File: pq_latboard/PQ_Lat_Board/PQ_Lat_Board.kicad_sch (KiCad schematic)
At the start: 20 parts, among them IC1 TCN75AVOA713, J1 Conn_01x11_MountingPin, J2 Conn_Coaxial

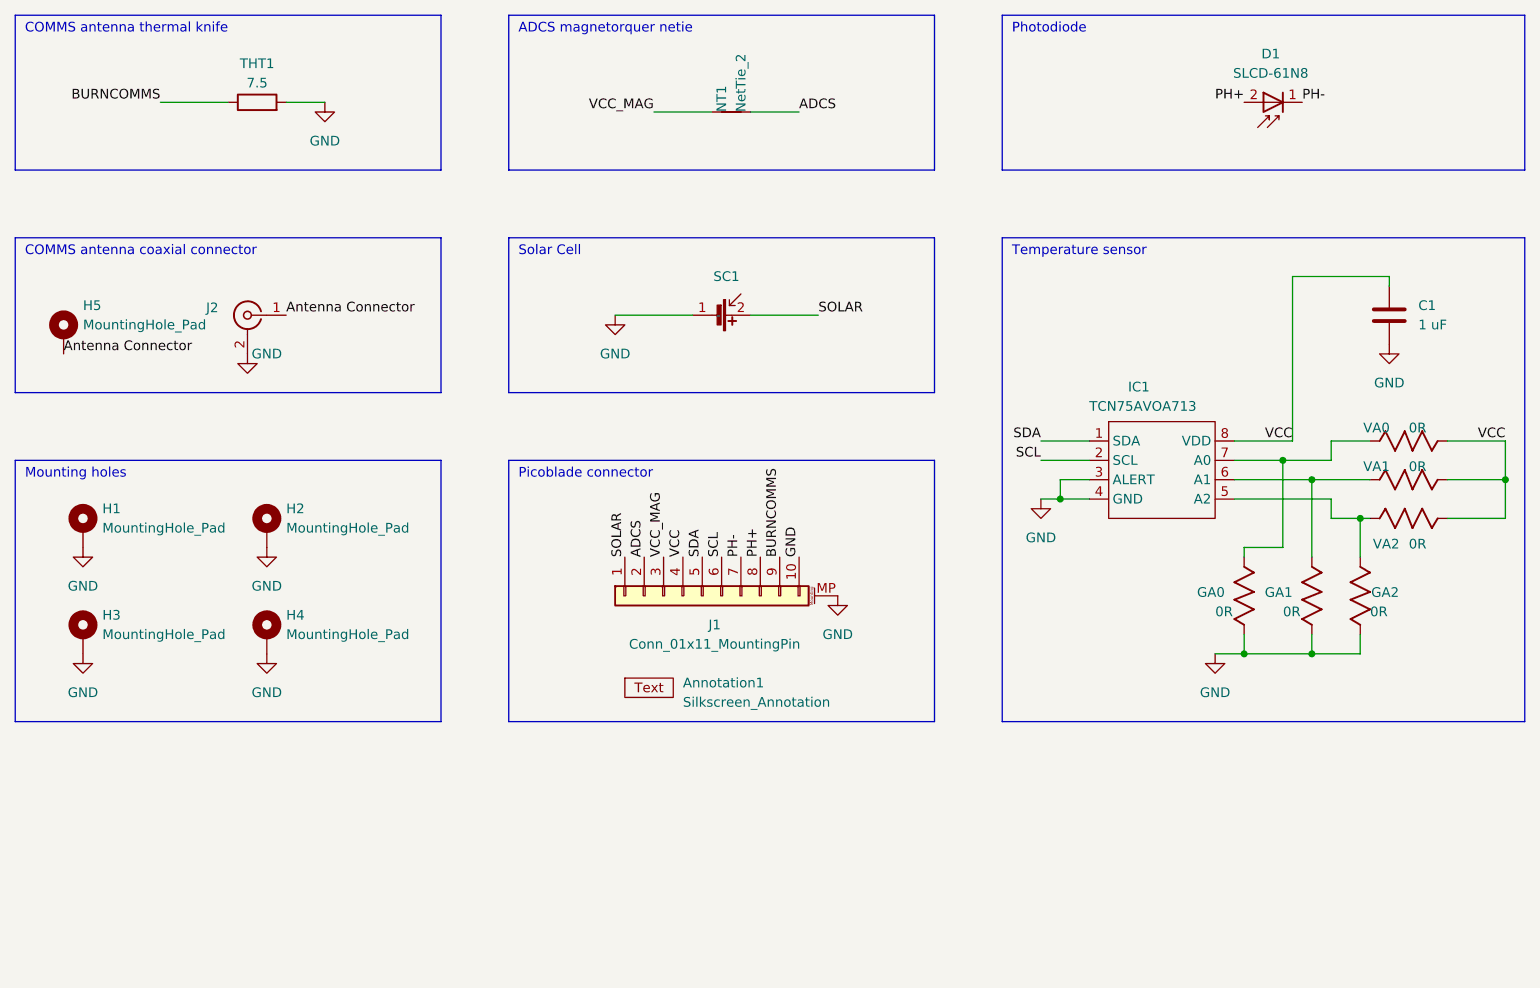
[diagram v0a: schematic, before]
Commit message: add names, bigger hole and mirror solar cell
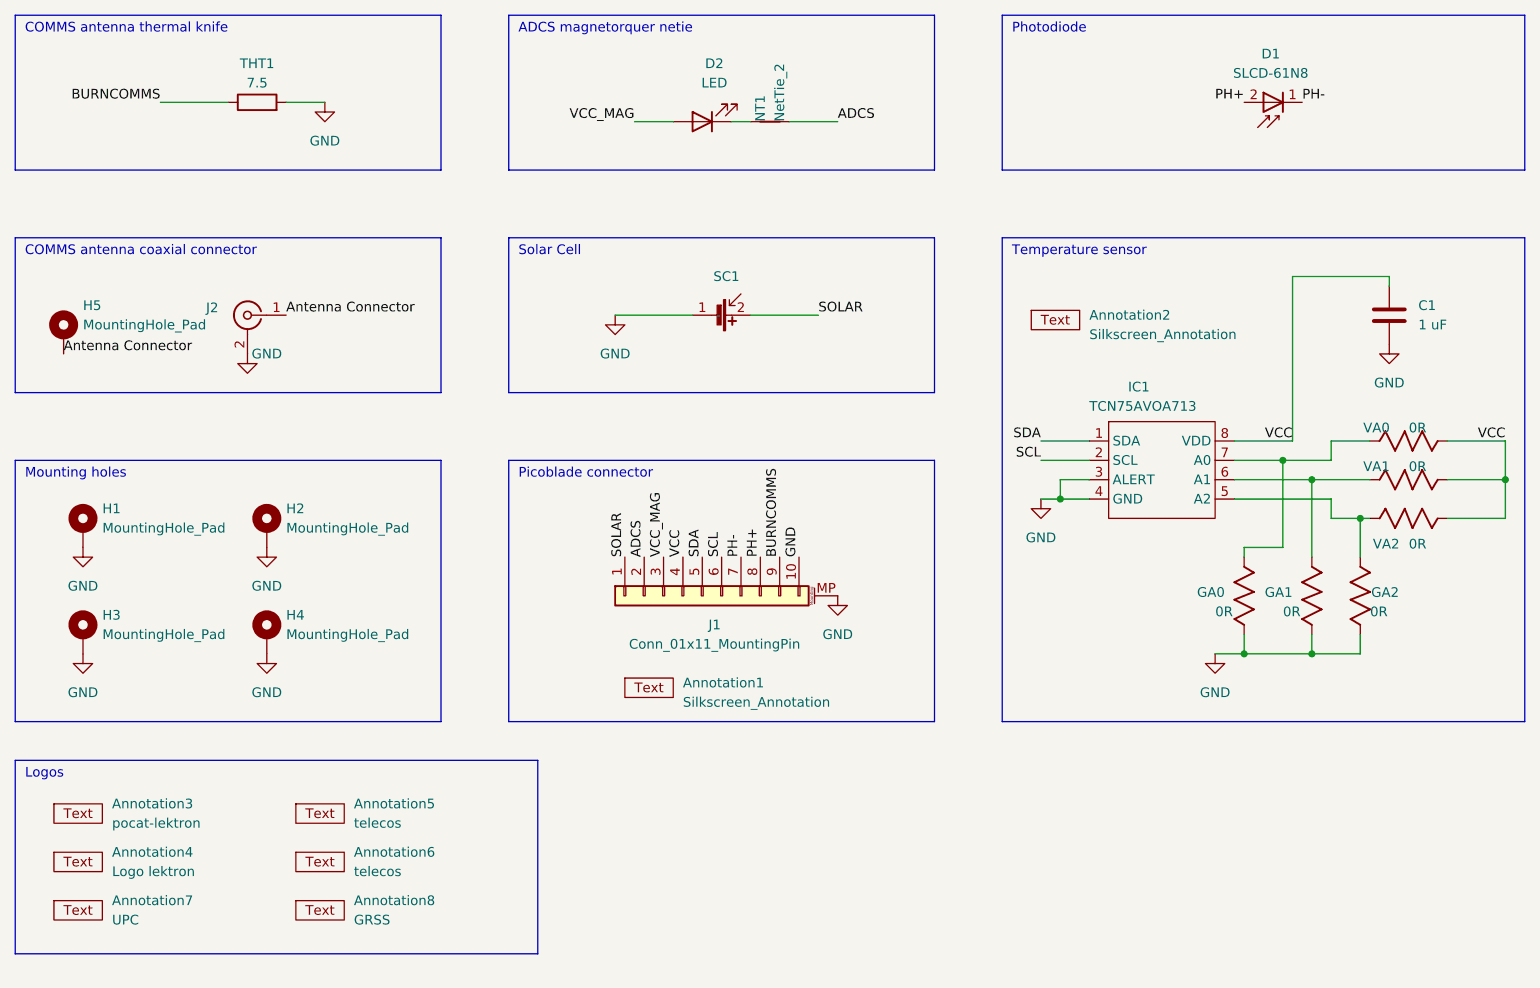
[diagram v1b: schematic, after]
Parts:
- added Annotation2: Silkscreen_Annotation, symbols-nsl:snail, symbol -nsl_symbols:Silkscreen_Annotation
- added Annotation3: pocat-lektron, symbols-nsl:pocat-lektron, symbol -nsl_symbols:Silkscreen_Annotation
- added Annotation4: Logo lektron, symbols-nsl:logo_pq, symbol -nsl_symbols:Silkscreen_Annotation
- added Annotation5: telecos, symbols-nsl:Telecos, symbol -nsl_symbols:Silkscreen_Annotation
- added Annotation6: telecos, symbols-nsl:NSL-small, symbol -nsl_symbols:Silkscreen_Annotation
- added Annotation7: UPC, symbols-nsl:UPC_small, symbol -nsl_symbols:Silkscreen_Annotation
- added Annotation8: GRSS, symbols-nsl:GRSS, symbol -nsl_symbols:Silkscreen_Annotation
- added D2: LED, LED_SMD:LED_0402_1005Metric, symbol Device:LED
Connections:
- net VCC_MAG: now also D2.2 (A); no longer NT1.1
- new net: D2.1 (K), NT1.1
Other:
- note added: "Logos"
- moved on the sheet: NT1

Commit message: Removed netie, updated SC footprint, trace reform, logo&name cleanup, footprint reconciled, DRC
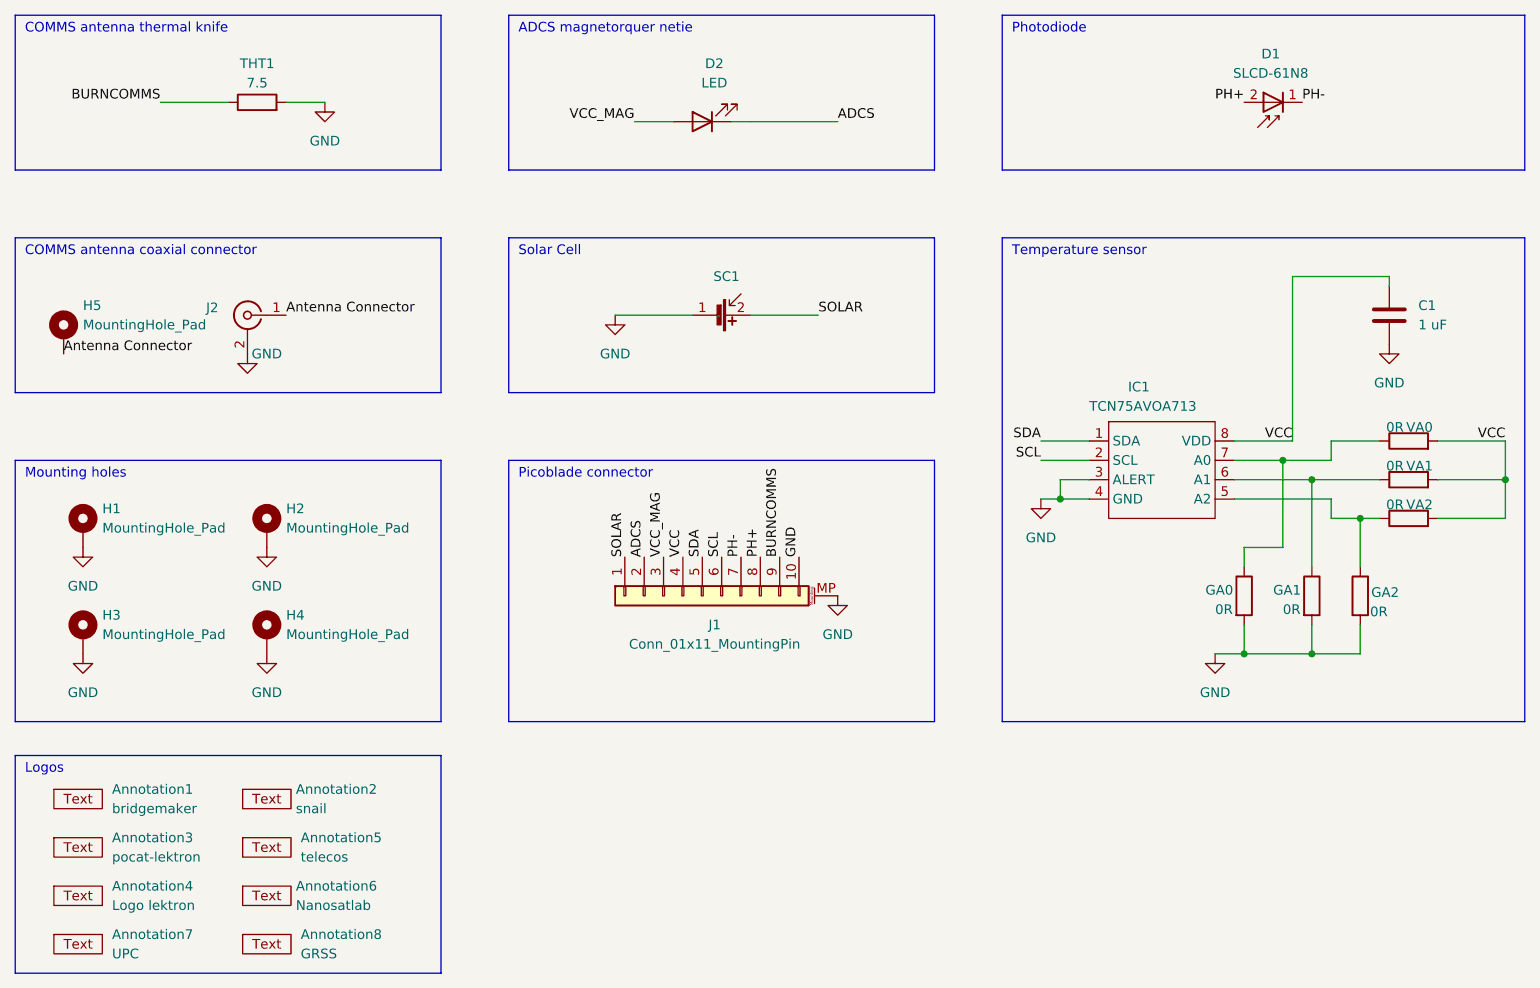
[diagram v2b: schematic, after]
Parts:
- removed NT1: NetTie_2, NetTie:NetTie-2_SMD_Pad0.5mm, symbol Device:NetTie_2
- Annotation1: value Silkscreen_Annotation -> bridgemaker; footprint -nsl_symbols:Bridgemaker -> symbols-nsl:Bridgemaker
- Annotation2: value Silkscreen_Annotation -> snail; footprint symbols-nsl:snail -> symbols-nsl:Snail
- Annotation3: footprint symbols-nsl:pocat-lektron -> symbols-nsl:pocat_lektron
- Annotation4: footprint symbols-nsl:logo_pq -> symbols-nsl:NSL_hexagon
- Annotation6: value telecos -> Nanosatlab
- D1: footprint -nsl_passive:SLCD-61N8 -> passive-nsl:SLCD-61N8
- GA0, GA1, GA2: symbol Lateral_board-altium-import:1_5k -> Device:R
- IC1: footprint -nsl_sensor:TCN75AVOA -> sensor-nsl:TCN75AVOA
- VA0, VA1, VA2: symbol Lateral_board-altium-import:0_5k -> Device:R
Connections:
- net ADCS: now also D2.1 (K)
- net GND: now also GA0.2, GA1.2, GA2.2; no longer GA0.1, GA1.1, GA2.1
- net at IC1.7 (A0), VA0.1: now also GA0.1; no longer GA0.2
- net at IC1.6 (A1), VA1.1: now also GA1.1; no longer GA1.2
- net at IC1.5 (A2), VA2.1: now also GA2.1; no longer GA2.2
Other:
- moved on the sheet: Annotation1, Annotation2, Annotation3, Annotation4, Annotation5, Annotation6, Annotation7, Annotation8

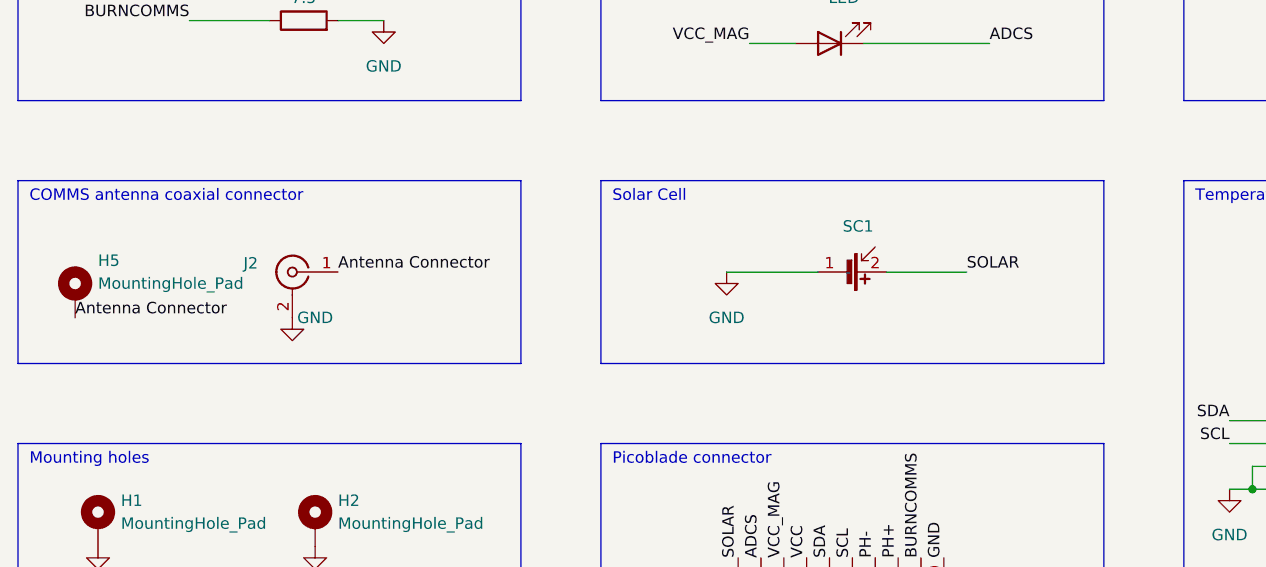
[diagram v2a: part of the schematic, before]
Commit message: Re-routed the SC, added new SC symbol in schematic, and added pad to solder the comms antenna inside the lateral.
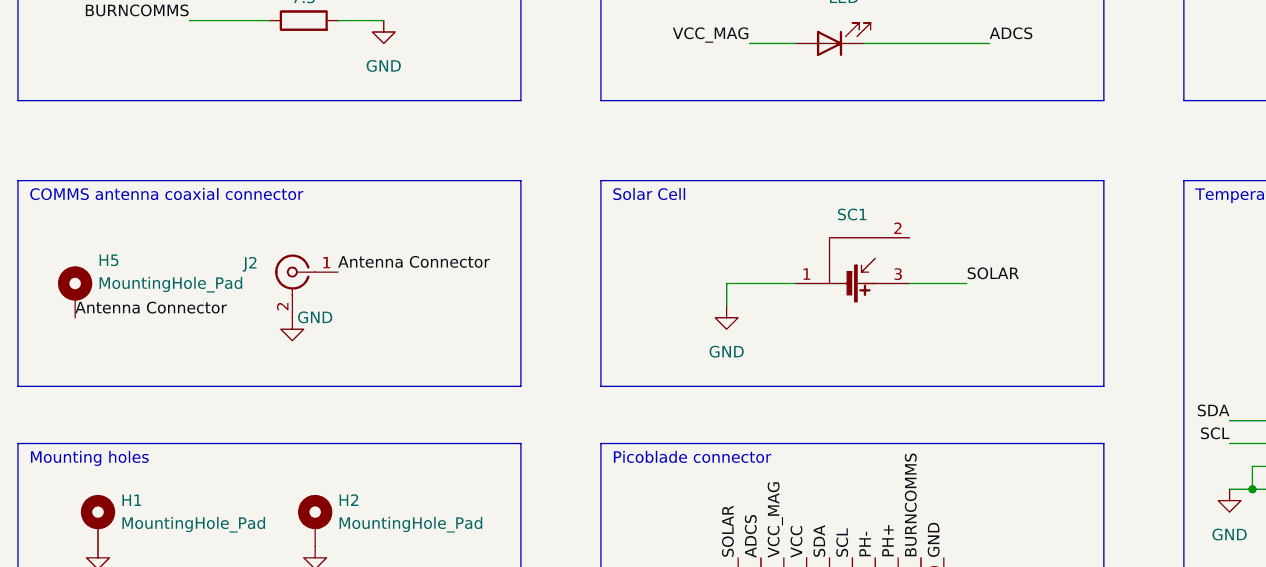
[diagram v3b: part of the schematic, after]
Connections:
- net SOLAR: now also SC1.3; no longer SC1.2
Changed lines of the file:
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@@
     (stroke (width 0.254) (type default))
   )
-  (polyline (pts (xy 114.3 82.55) (xy 114.3 102.87))
+  (polyline (pts (xy 114.3 82.55) (xy 114.3 105.41))
     (stroke (width 0) (type default))
   )
@@
     (stroke (width 0) (type default))
   )
-  (wire (pts (xy 128.27 92.71) (xy 138.43 92.71))
-    (stroke (width 0) (type default))
-  )
-  (polyline (pts (xy 114.3 102.87) (xy 170.18 102.87))
+  (polyline (pts (xy 114.3 105.41) (xy 170.18 105.41))
     (stroke (width 0) (type default))
   )
@@
     (stroke (width 0) (type default))
   )
-  (wire (pts (xy 146.05 92.71) (xy 154.94 92.71))
+  (wire (pts (xy 135.89 93.98) (xy 128.27 93.98))
     (stroke (width 0) (type default))
   )
@@
     (stroke (width 0.254) (type default))
   )
-  (polyline (pts (xy 170.18 82.55) (xy 170.18 102.87))
+  (polyline (pts (xy 170.18 82.55) (xy 170.18 105.41))
     (stroke (width 0) (type default))
   )
@@
     (stroke (width 0) (type default))
   )
+  (wire (pts (xy 128.27 93.98) (xy 128.27 96.52))
+    (stroke (width 0) (type default))
+  )
+  (wire (pts (xy 148.59 93.98) (xy 154.94 93.98))
+    (stroke (width 0) (type default))
+  )
   (wire (pts (xy 143.51 67.31) (xy 146.05 67.31))
     (stroke (width 0) (type default))
@@
     (stroke (width 0) (type default))
   )
-  (polyline (pts (xy 49.53 82.55) (xy 49.53 102.87))
+  (polyline (pts (xy 49.53 82.55) (xy 49.53 105.41))
     (stroke (width 0) (type default))
   )
@@
     (stroke (width 0) (type default))
   )
-  (polyline (pts (xy 105.41 102.87) (xy 105.41 82.55))
+  (polyline (pts (xy 105.41 105.41) (xy 105.41 82.55))
     (stroke (width 0) (type default))
   )
@@
     (stroke (width 0.254) (type default))
   )
-  (polyline (pts (xy 49.53 102.87) (xy 105.41 102.87))
+  (polyline (pts (xy 49.53 105.41) (xy 105.41 105.41))
     (stroke (width 0) (type default))
   )
@@
     (effects (font (size 1.27 1.27)) (justify left bottom))
   )
-  (label "SOLAR" (at 154.94 92.71 0) (fields_autoplaced)
+  (label "SOLAR" (at 154.94 93.98 0) (fields_autoplaced)
     (effects (font (size 1.27 1.27)) (justify left bottom))
   )
@@
     )
   )
-  (symbol (lib_name "GND_2") (lib_id "power:GND") (at 128.27 92.71 0) (unit 1)
-    (in_bom yes) (on_board yes) (dnp no) (fields_autoplaced)
-    (property "Reference" "#PWR0111" (at 128.27 99.06 0)
-      (effects (font (size 1.27 1.27)) hide)
-    )
-    (property "Value" "GND" (at 128.27 97.79 0)
-      (effects (font (size 1.27 1.27)))
-    )
-    (property "Footprint" "" (at 128.27 92.71 0)
-      (effects (font (size 1.27 1.27)) hide)
-    )
-    (property "Datasheet" "" (at 128.27 92.71 0)
+  (symbol (lib_name "GND_2") (lib_id "power:GND") (at 128.27 96.52 0) (unit 1)
+    (in_bom yes) (on_board yes) (dnp no) (fields_autoplaced)
+    (property "Reference" "#PWR0111" (at 128.27 102.87 0)
+      (effects (font (size 1.27 1.27)) hide)
+    )
+    (property "Value" "GND" (at 128.27 101.6 0)
+      (effects (font (size 1.27 1.27)))
+    )
+    (property "Footprint" "" (at 128.27 96.52 0)
+      (effects (font (size 1.27 1.27)) hide)
+    )
+    (property "Datasheet" "" (at 128.27 96.52 0)
       (effects (font (size 1.27 1.27)) hide)
     )
@@
     )
   )
+  (symbol (lib_id "power-nsl:S3040_CIC") (at 142.24 93.98 270) (unit 1)
+    (in_bom yes) (on_board yes) (dnp no) (fields_autoplaced)
+    (property "Reference" "SC1" (at 142.24 86.36 90)
+      (effects (font (size 1.27 1.27)))
+    )
+    (property "Value" "~" (at 142.24 93.98 0)
+      (effects (font (size 1.27 1.27)))
+    )
+    (property "Footprint" "power-nsl:Lighttricity_S3040_CIC" (at 142.24 93.98 0)
+      (effects (font (size 1.27 1.27)) hide)
+    )
+    (property "Datasheet" "" (at 142.24 93.98 0)
+      (effects (font (size 1.27 1.27)) hide)
+    )
+    (pin "2")
+    (pin "1")
+    (pin "3")
+    (instances
+      (project "PQ_Lat_Board"
+        (path "/4da848d5-e65a-4ace-88f8-d9d6d6b9afa2"
+          (reference "SC1") (unit 1)
+        )
+      )
+    )
+  )
   (symbol (lib_id "-nsl_symbols:Silkscreen_Annotation") (at 55.88 168.275 0) (unit 1)
     (in_bom yes) (on_board yes) (dnp no) (fields_autoplaced)
@@
         )
       )
-    )
-  )
-  (symbol (lib_id "power-nsl:S3040_CIC") (at 142.24 92.71 270) (unit 1)
-    (in_bom yes) (on_board yes) (dnp no) (fields_autoplaced)
-    (property "Reference" "SC1" (at 142.875 87.63 90)
-      (effects (font (size 1.27 1.27)))
-    )
-    (property "Value" "~" (at 142.24 92.71 0)
-      (effects (font (size 1.27 1.27)))
-    )
-    (property "Footprint" "power-nsl:Lighttricity_S3040_CIC" (at 142.24 92.71 0)
-      (effects (font (size 1.27 1.27)) hide)
-    )
-    (property "Datasheet" "" (at 142.24 92.71 0)
-      (effects (font (size 1.27 1.27)) hide)
-    )
-    (pin "1")
-    (pin "2")
-    (instances
-      (project "PQ_Lat_Board"
-        (path "/4da848d5-e65a-4ace-88f8-d9d6d6b9afa2"
-          (reference "SC1") (unit 1)
-        )
-      )
